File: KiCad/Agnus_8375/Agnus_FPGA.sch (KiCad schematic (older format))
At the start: 22 parts, among them J6 Conn_01x01, U1 10M02SCU169C8G, U2 LM1117-3.3

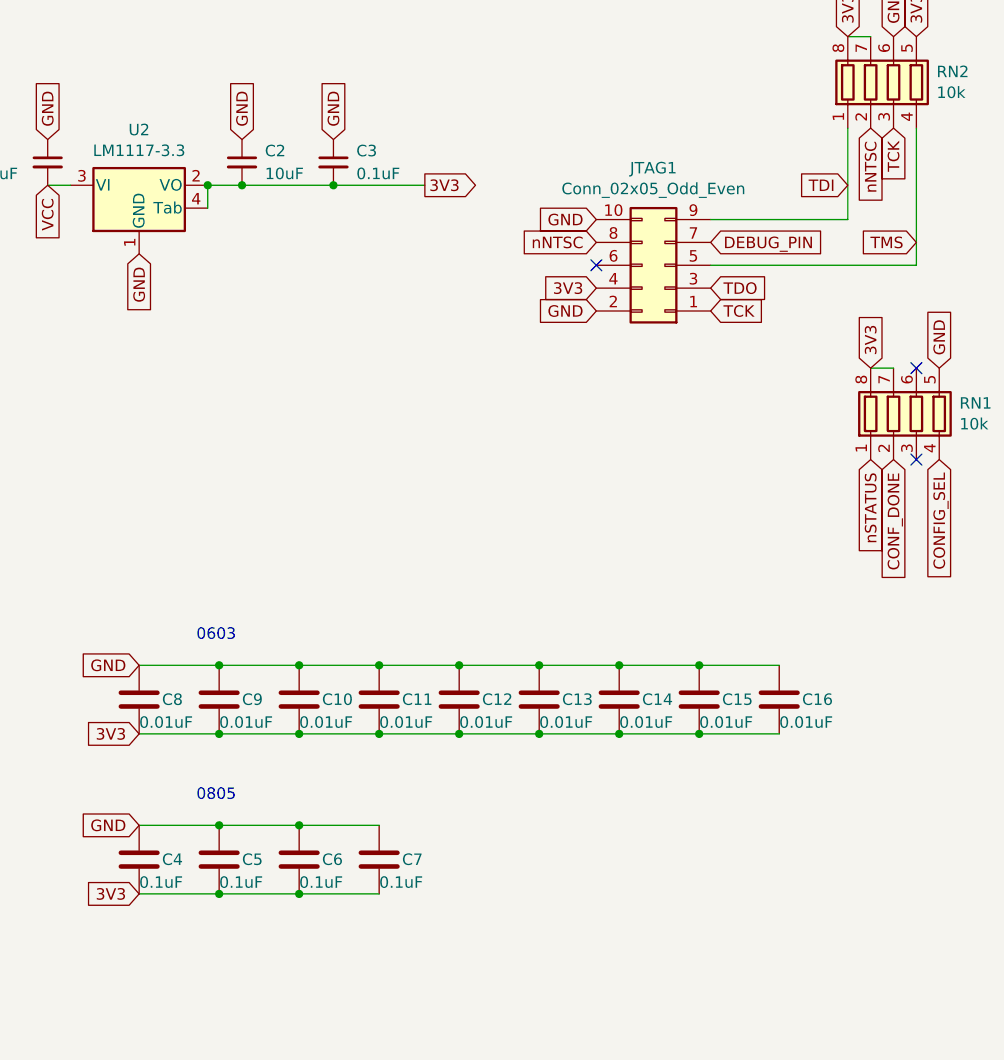
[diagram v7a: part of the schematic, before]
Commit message: Added more decoupling caps
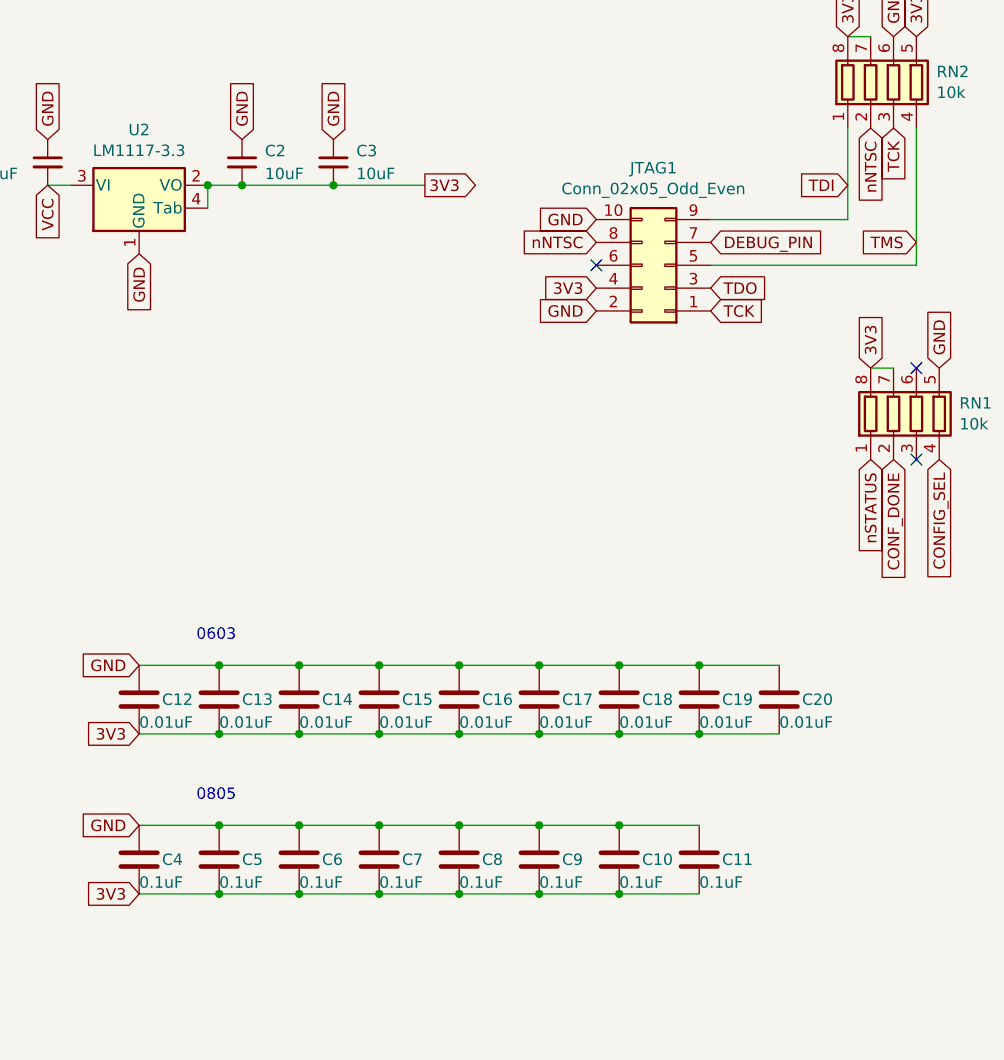
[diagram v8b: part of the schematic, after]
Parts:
- added C11, C4, C5, C8: 0.1uF, Capacitor_SMD:C_0805_2012Metric_Pad1.15x1.40mm_HandSolder, symbol Device:C
- C3: value 0.1uF -> 10uF; footprint Capacitor_SMD:C_0805_2012Metric_Pad1.15x1.40mm_HandSolder -> Capacitor_SMD:C_1206_3216Metric_Pad1.42x1.75mm_HandSolder
- renumbered C7 to C10, C8 to C12, C9 to C13, C10 to C14, C11 to C15, C12 to C16, C13 to C17, C14 to C18, C15 to C19, C16 to C20, C4 to C6, C5 to C7, C6 to C9
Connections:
- net 3V3: now also C11.2, C4.2, C5.2, C8.2
- net GND: now also C11.1, C4.1, C5.1, C8.1
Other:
- moved on the sheet: C10, C6, C7, C9
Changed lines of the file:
@@
 Text GLabel 7700 1300 1    50   Input ~ 0
 GND
-$Comp
-L Device:C_Small C3
-U 1 1 60C66617
-P 8100 1400
-F 0 "C3" H 8200 1450 50  0000 L CNN
-F 1 "0.1uF" H 8200 1350 50  0000 L CNN
-F 2 "Capacitor_SMD:C_0805_2012Metric_Pad1.15x1.40mm_HandSolder" H 8100 1400 50  0001 C CNN
-F 3 "~" H 8100 1400 50  0001 C CNN
-	1    8100 1400
-	1    0    0    -1
-$EndComp
 Text GLabel 8100 1300 1    50   Input ~ 0
 GND
@@
 Connection ~ 7550 1500
 Connection ~ 7700 1500
-Wire Wire Line
-	7700 1500 8100 1500
-Wire Wire Line
-	8100 1500 8500 1500
-Connection ~ 8100 1500
 Text GLabel 950  2550 0    50   Input ~ 0
 TMS
@@
 P 10050 3750
 AR Path="/60CC8EF6" Ref="C?"  Part="1"
-AR Path="/608A10F5/60CC8EF6" Ref="C16"  Part="1"
-F 0 "C16" H 10150 3750 50  0000 L CNN
+AR Path="/608A10F5/60CC8EF6" Ref="C20"  Part="1"
+F 0 "C20" H 10150 3750 50  0000 L CNN
 F 1 "0.01uF" H 10050 3650 50  0000 L CNN
 F 2 "Capacitor_SMD:C_0603_1608Metric_Pad1.05x0.95mm_HandSolder" H 10088 3600 50  0001 C CNN
@@
 P 9700 3750
 AR Path="/60CC8EFC" Ref="C?"  Part="1"
-AR Path="/608A10F5/60CC8EFC" Ref="C15"  Part="1"
-F 0 "C15" H 9800 3750 50  0000 L CNN
+AR Path="/608A10F5/60CC8EFC" Ref="C19"  Part="1"
+F 0 "C19" H 9800 3750 50  0000 L CNN
 F 1 "0.01uF" H 9700 3650 50  0000 L CNN
 F 2 "Capacitor_SMD:C_0603_1608Metric_Pad1.05x0.95mm_HandSolder" H 9738 3600 50  0001 C CNN
@@
 P 9350 3750
 AR Path="/60CC8F02" Ref="C?"  Part="1"
-AR Path="/608A10F5/60CC8F02" Ref="C14"  Part="1"
-F 0 "C14" H 9450 3750 50  0000 L CNN
+AR Path="/608A10F5/60CC8F02" Ref="C18"  Part="1"
+F 0 "C18" H 9450 3750 50  0000 L CNN
 F 1 "0.01uF" H 9350 3650 50  0000 L CNN
 F 2 "Capacitor_SMD:C_0603_1608Metric_Pad1.05x0.95mm_HandSolder" H 9388 3600 50  0001 C CNN
@@
 L Device:C C?
 U 1 1 60CC8F0E
-P 8300 4450
+P 9350 4450
 AR Path="/60CC8F0E" Ref="C?"  Part="1"
-AR Path="/608A10F5/60CC8F0E" Ref="C7"  Part="1"
-F 0 "C7" H 8400 4450 50  0000 L CNN
-F 1 "0.1uF" H 8300 4350 50  0000 L CNN
-F 2 "Capacitor_SMD:C_0805_2012Metric_Pad1.15x1.40mm_HandSolder" H 8338 4300 50  0001 C CNN
-F 3 "~" H 8300 4450 50  0001 C CNN
-	1    8300 4450
+AR Path="/608A10F5/60CC8F0E" Ref="C10"  Part="1"
+F 0 "C10" H 9450 4450 50  0000 L CNN
+F 1 "0.1uF" H 9350 4350 50  0000 L CNN
+F 2 "Capacitor_SMD:C_0805_2012Metric_Pad1.15x1.40mm_HandSolder" H 9388 4300 50  0001 C CNN
+F 3 "~" H 9350 4450 50  0001 C CNN
+	1    9350 4450
 	1    0    0    -1
 $EndComp
@@
 L Device:C C?
 U 1 1 607ACE36
-P 7600 4450
+P 8300 4450
 AR Path="/607ACE36" Ref="C?"  Part="1"
-AR Path="/608A10F5/607ACE36" Ref="C5"  Part="1"
-F 0 "C5" H 7700 4450 50  0000 L CNN
-F 1 "0.1uF" H 7600 4350 50  0000 L CNN
-F 2 "Capacitor_SMD:C_0805_2012Metric_Pad1.15x1.40mm_HandSolder" H 7638 4300 50  0001 C CNN
-F 3 "~" H 7600 4450 50  0001 C CNN
-	1    7600 4450
+AR Path="/608A10F5/607ACE36" Ref="C7"  Part="1"
+F 0 "C7" H 8400 4450 50  0000 L CNN
+F 1 "0.1uF" H 8300 4350 50  0000 L CNN
+F 2 "Capacitor_SMD:C_0805_2012Metric_Pad1.15x1.40mm_HandSolder" H 8338 4300 50  0001 C CNN
+F 3 "~" H 8300 4450 50  0001 C CNN
+	1    8300 4450
 	1    0    0    -1
 $EndComp
@@
 P 7250 3750
 AR Path="/60636E2E" Ref="C?"  Part="1"
-AR Path="/608A10F5/60636E2E" Ref="C8"  Part="1"
-F 0 "C8" H 7350 3750 50  0000 L CNN
+AR Path="/608A10F5/60636E2E" Ref="C12"  Part="1"
+F 0 "C12" H 7350 3750 50  0000 L CNN
 F 1 "0.01uF" H 7250 3650 50  0000 L CNN
 F 2 "Capacitor_SMD:C_0603_1608Metric_Pad1.05x0.95mm_HandSolder" H 7288 3600 50  0001 C CNN
@@
 P 7600 3750
 AR Path="/60637476" Ref="C?"  Part="1"
-AR Path="/608A10F5/60637476" Ref="C9"  Part="1"
-F 0 "C9" H 7700 3750 50  0000 L CNN
+AR Path="/608A10F5/60637476" Ref="C13"  Part="1"
+F 0 "C13" H 7700 3750 50  0000 L CNN
 F 1 "0.01uF" H 7600 3650 50  0000 L CNN
 F 2 "Capacitor_SMD:C_0603_1608Metric_Pad1.05x0.95mm_HandSolder" H 7638 3600 50  0001 C CNN
@@
 P 8300 3750
 AR Path="/60637B30" Ref="C?"  Part="1"
-AR Path="/608A10F5/60637B30" Ref="C11"  Part="1"
-F 0 "C11" H 8400 3750 50  0000 L CNN
+AR Path="/608A10F5/60637B30" Ref="C15"  Part="1"
+F 0 "C15" H 8400 3750 50  0000 L CNN
 F 1 "0.01uF" H 8300 3650 50  0000 L CNN
 F 2 "Capacitor_SMD:C_0603_1608Metric_Pad1.05x0.95mm_HandSolder" H 8338 3600 50  0001 C CNN
@@
 P 8650 3750
 AR Path="/60638427" Ref="C?"  Part="1"
-AR Path="/608A10F5/60638427" Ref="C12"  Part="1"
-F 0 "C12" H 8750 3750 50  0000 L CNN
+AR Path="/608A10F5/60638427" Ref="C16"  Part="1"
+F 0 "C16" H 8750 3750 50  0000 L CNN
 F 1 "0.01uF" H 8650 3650 50  0000 L CNN
 F 2 "Capacitor_SMD:C_0603_1608Metric_Pad1.05x0.95mm_HandSolder" H 8688 3600 50  0001 C CNN
@@
 L Device:C C?
 U 1 1 60785965
-P 7250 4450
+P 7950 4450
 AR Path="/60785965" Ref="C?"  Part="1"
-AR Path="/608A10F5/60785965" Ref="C4"  Part="1"
-F 0 "C4" H 7350 4450 50  0000 L CNN
-F 1 "0.1uF" H 7250 4350 50  0000 L CNN
-F 2 "Capacitor_SMD:C_0805_2012Metric_Pad1.15x1.40mm_HandSolder" H 7288 4300 50  0001 C CNN
-F 3 "~" H 7250 4450 50  0001 C CNN
-	1    7250 4450
+AR Path="/608A10F5/60785965" Ref="C6"  Part="1"
+F 0 "C6" H 8050 4450 50  0000 L CNN
+F 1 "0.1uF" H 7950 4350 50  0000 L CNN
+F 2 "Capacitor_SMD:C_0805_2012Metric_Pad1.15x1.40mm_HandSolder" H 7988 4300 50  0001 C CNN
+F 3 "~" H 7950 4450 50  0001 C CNN
+	1    7950 4450
 	1    0    0    -1
 $EndComp
@@
 L Device:C C?
 U 1 1 608291F3
-P 7950 4450
+P 9000 4450
 AR Path="/608291F3" Ref="C?"  Part="1"
-AR Path="/608A10F5/608291F3" Ref="C6"  Part="1"
-F 0 "C6" H 8050 4450 50  0000 L CNN
-F 1 "0.1uF" H 7950 4350 50  0000 L CNN
-F 2 "Capacitor_SMD:C_0805_2012Metric_Pad1.15x1.40mm_HandSolder" H 7988 4300 50  0001 C CNN
-F 3 "~" H 7950 4450 50  0001 C CNN
-	1    7950 4450
+AR Path="/608A10F5/608291F3" Ref="C9"  Part="1"
+F 0 "C9" H 9100 4450 50  0000 L CNN
+F 1 "0.1uF" H 9000 4350 50  0000 L CNN
+F 2 "Capacitor_SMD:C_0805_2012Metric_Pad1.15x1.40mm_HandSolder" H 9038 4300 50  0001 C CNN
+F 3 "~" H 9000 4450 50  0001 C CNN
+	1    9000 4450
 	1    0    0    -1
 $EndComp
@@
 P 9000 3750
 AR Path="/60898D1D" Ref="C?"  Part="1"
-AR Path="/608A10F5/60898D1D" Ref="C13"  Part="1"
-F 0 "C13" H 9100 3750 50  0000 L CNN
+AR Path="/608A10F5/60898D1D" Ref="C17"  Part="1"
+F 0 "C17" H 9100 3750 50  0000 L CNN
 F 1 "0.01uF" H 9000 3650 50  0000 L CNN
 F 2 "Capacitor_SMD:C_0603_1608Metric_Pad1.05x0.95mm_HandSolder" H 9038 3600 50  0001 C CNN
@@
 P 7950 3750
 AR Path="/608A7236" Ref="C?"  Part="1"
-AR Path="/608A10F5/608A7236" Ref="C10"  Part="1"
-F 0 "C10" H 8050 3750 50  0000 L CNN
+AR Path="/608A10F5/608A7236" Ref="C14"  Part="1"
+F 0 "C14" H 8050 3750 50  0000 L CNN
 F 1 "0.01uF" H 7950 3650 50  0000 L CNN
 F 2 "Capacitor_SMD:C_0603_1608Metric_Pad1.05x0.95mm_HandSolder" H 7988 3600 50  0001 C CNN
@@
 Wire Wire Line
 	8650 3900 9000 3900
+$Comp
+L Device:C C?
+U 1 1 608425C5
+P 7600 4450
+AR Path="/608425C5" Ref="C?"  Part="1"
+AR Path="/608A10F5/608425C5" Ref="C5"  Part="1"
+F 0 "C5" H 7700 4450 50  0000 L CNN
+F 1 "0.1uF" H 7600 4350 50  0000 L CNN
+F 2 "Capacitor_SMD:C_0805_2012Metric_Pad1.15x1.40mm_HandSolder" H 7638 4300 50  0001 C CNN
+F 3 "~" H 7600 4450 50  0001 C CNN
+	1    7600 4450
+	1    0    0    -1
+$EndComp
+$Comp
+L Device:C C?
+U 1 1 6084338C
+P 8650 4450
+AR Path="/6084338C" Ref="C?"  Part="1"
+AR Path="/608A10F5/6084338C" Ref="C8"  Part="1"
+F 0 "C8" H 8750 4450 50  0000 L CNN
+F 1 "0.1uF" H 8650 4350 50  0000 L CNN
+F 2 "Capacitor_SMD:C_0805_2012Metric_Pad1.15x1.40mm_HandSolder" H 8688 4300 50  0001 C CNN
+F 3 "~" H 8650 4450 50  0001 C CNN
+	1    8650 4450
+	1    0    0    -1
+$EndComp
+$Comp
+L Device:C C?
+U 1 1 6084459F
+P 9700 4450
+AR Path="/6084459F" Ref="C?"  Part="1"
+AR Path="/608A10F5/6084459F" Ref="C11"  Part="1"
+F 0 "C11" H 9800 4450 50  0000 L CNN
+F 1 "0.1uF" H 9700 4350 50  0000 L CNN
+F 2 "Capacitor_SMD:C_0805_2012Metric_Pad1.15x1.40mm_HandSolder" H 9738 4300 50  0001 C CNN
+F 3 "~" H 9700 4450 50  0001 C CNN
+	1    9700 4450
+	1    0    0    -1
+$EndComp
+Wire Wire Line
+	8300 4300 8650 4300
+Connection ~ 8300 4300
+Connection ~ 8650 4300
+Wire Wire Line
+	8650 4300 9000 4300
+Connection ~ 9000 4300
+Wire Wire Line
+	9000 4300 9350 4300
+Wire Wire Line
+	8300 4600 8650 4600
+Connection ~ 8300 4600
+Connection ~ 8650 4600
+Wire Wire Line
+	8650 4600 9000 4600
+Connection ~ 9000 4600
+Wire Wire Line
+	9000 4600 9350 4600
+$Comp
+L Device:C C?
+U 1 1 6085C631
+P 7250 4450
+AR Path="/6085C631" Ref="C?"  Part="1"
+AR Path="/608A10F5/6085C631" Ref="C4"  Part="1"
+F 0 "C4" H 7350 4450 50  0000 L CNN
+F 1 "0.1uF" H 7250 4350 50  0000 L CNN
+F 2 "Capacitor_SMD:C_0805_2012Metric_Pad1.15x1.40mm_HandSolder" H 7288 4300 50  0001 C CNN
+F 3 "~" H 7250 4450 50  0001 C CNN
+	1    7250 4450
+	1    0    0    -1
+$EndComp
+Wire Wire Line
+	9350 4300 9700 4300
+Connection ~ 9350 4300
+Wire Wire Line
+	9350 4600 9700 4600
+Connection ~ 9350 4600
+$Comp
+L Device:C_Small C3
+U 1 1 6086B673
+P 8100 1400
+F 0 "C3" H 8200 1450 50  0000 L CNN
+F 1 "10uF" H 8200 1350 50  0000 L CNN
+F 2 "Capacitor_SMD:C_1206_3216Metric_Pad1.42x1.75mm_HandSolder" H 8100 1400 50  0001 C CNN
+F 3 "~" H 8100 1400 50  0001 C CNN
+	1    8100 1400
+	1    0    0    -1
+$EndComp
+Wire Wire Line
+	7700 1500 8100 1500
+Connection ~ 8100 1500
+Wire Wire Line
+	8100 1500 8500 1500
 $EndSCHEMATC
